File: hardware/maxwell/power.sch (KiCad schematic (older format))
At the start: 50 parts, among them J7 Dynamo Input, J9 Battery, Q2 PSMN5R4-25YLD, Q3 DMG9926UDM, Q4 NTR1P02T1, Q5 NTR1P02T1, U1 MCP1501, U10 MIC39102, U11 AP9101C-SOT-25, U12 INA219AID, U13 PCF8593, U3 TPS2113, U4 PCA9536D, U6 AD7991, U8 TLP188, U9 Buck Regulator

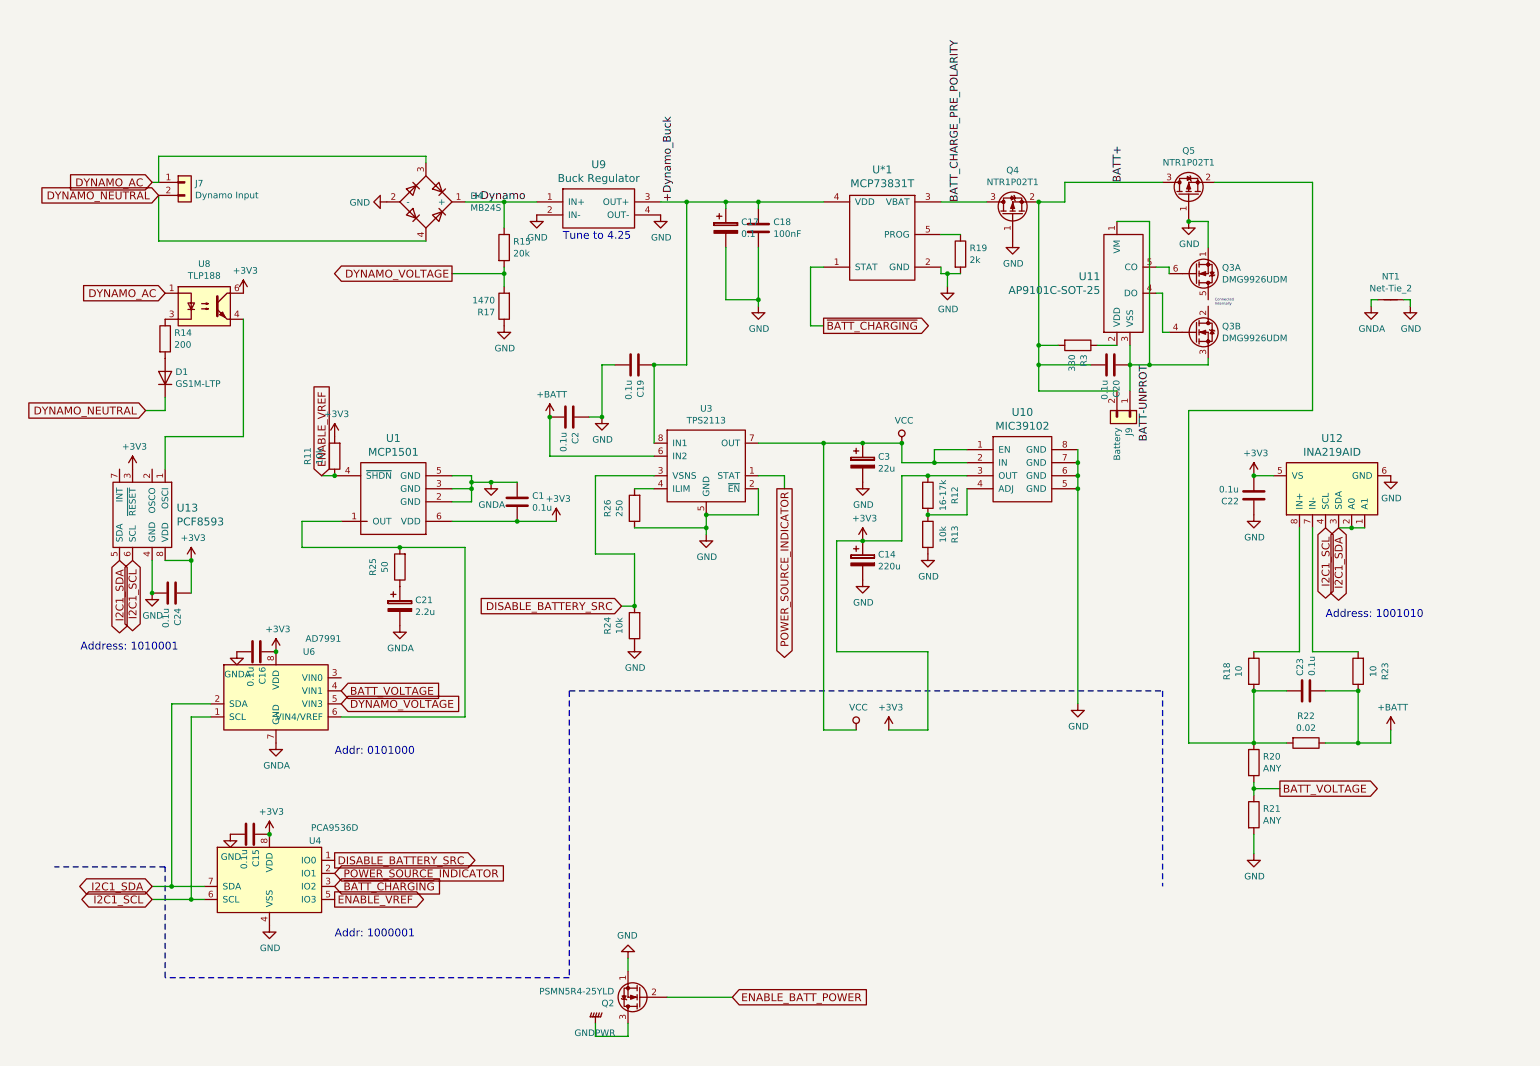
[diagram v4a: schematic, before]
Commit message: Revision 1.8a
* Collects regulated dynamo voltage via ADC channel 0.
* Swaps default power source from VBATT to VDYNAMO.  When charging, the
battery may have exactly the same voltage as the dynamo due to voltage
pulldown.  During such a scenario, we should use the dynamo.
* Adds previously missing pulldown resistor for open drain speed
input.
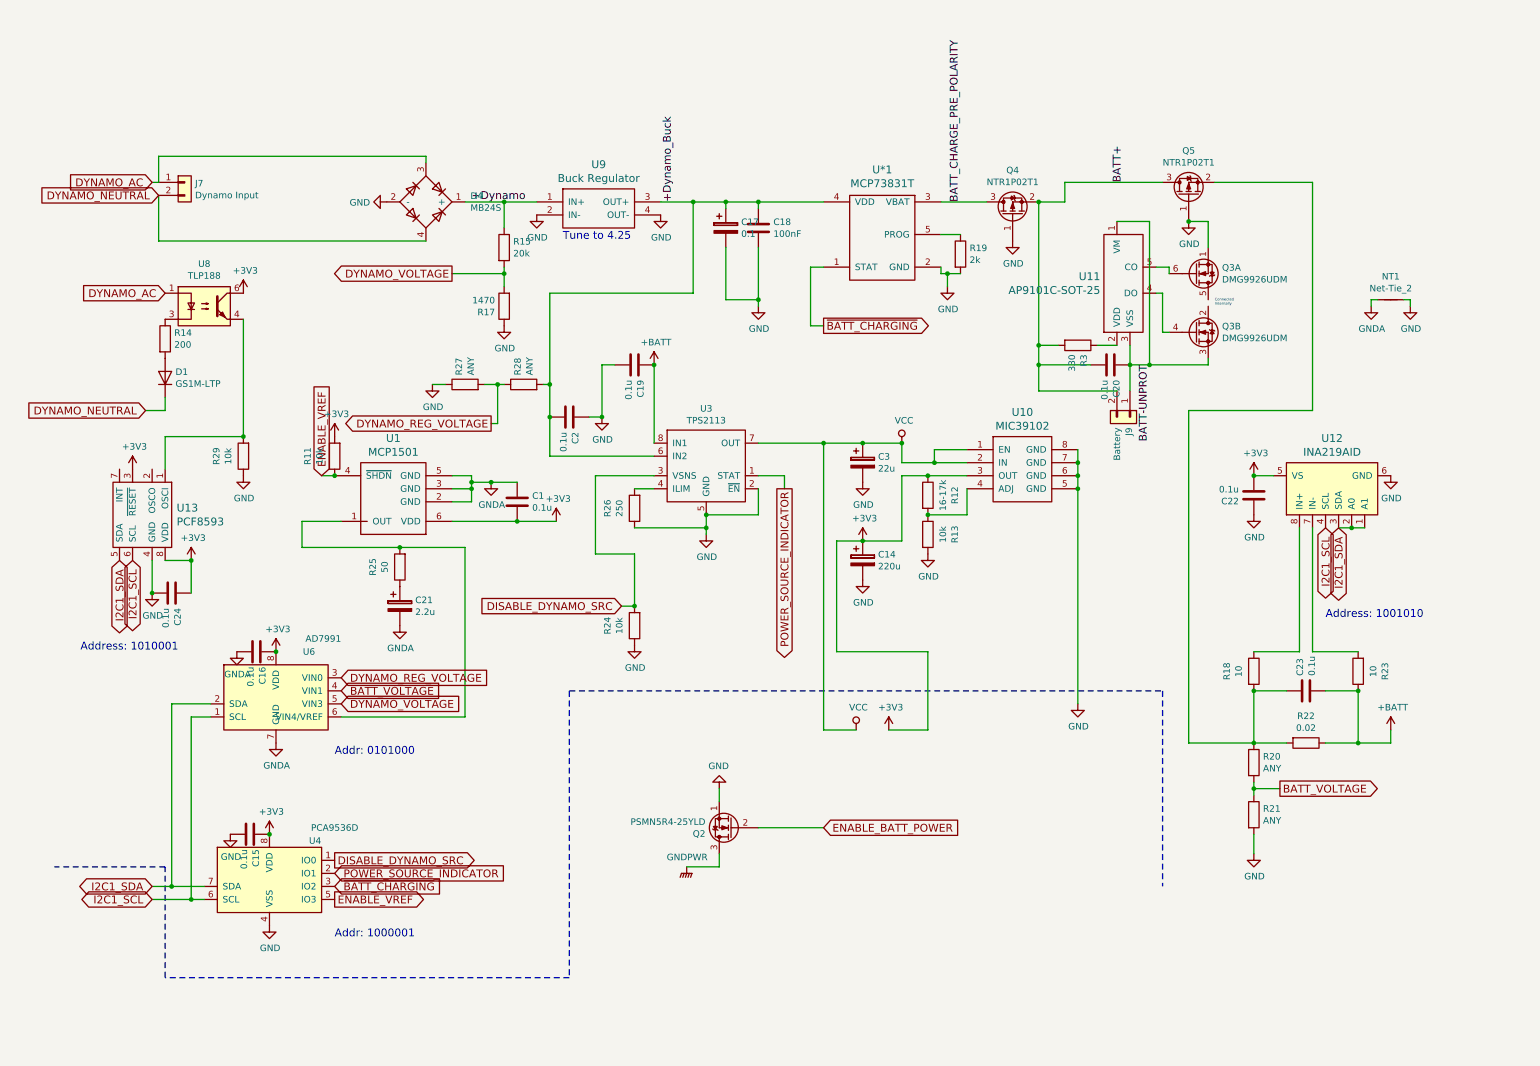
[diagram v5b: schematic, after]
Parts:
- added R27, R28: ANY, coddingtonbear:0805_Milling, symbol maxwell-rescue:R-RESCUE-maxwell
- added R29: 10k, coddingtonbear:0805_Milling, symbol maxwell-rescue:R-RESCUE-maxwell
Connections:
- net +BATT: now also C19.2, U3.8 (IN1); no longer C2.1, U3.6 (IN2)
- net +Dynamo_Buck: now also C2.1, U3.6 (IN2), R28.2; no longer C19.2, U3.8 (IN1)
- net GND: now also R27.1, R29.1
- net at U13.1 (OSCI), U8.4: now also R29.2
- net DYNAMO_REG_VOLTAGE: now reaches U6.3 (VIN0)
- net DYNAMO_REG_VOLTAGE: now also R27.2, R28.1
- net DISABLE_BATTERY_SRC renamed DISABLE_DYNAMO_SRC
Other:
- moved on the sheet: Q2
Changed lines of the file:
@@
 $EndComp
 Wire Wire Line
-	4900 7650 4650 7650
-Wire Wire Line
-	4650 7650 4650 7550
-Wire Wire Line
-	4900 7550 4900 7650
-Text GLabel 5700 7350 2    60   Input ~ 0
+	5600 6350 5350 6350
+Wire Wire Line
+	5600 6250 5600 6350
+Text GLabel 6400 6050 2    60   Input ~ 0
 ENABLE_BATT_POWER
 $Comp
 L maxwell-rescue:GND-RESCUE-maxwell #PWR050
 U 1 1 5A2580F1
-P 4900 7050
-F 0 "#PWR050" H 4900 6800 50  0001 C CNN
-F 1 "GND" H 4905 6877 50  0000 C CNN
-F 2 "" H 4900 7050 50  0001 C CNN
-F 3 "" H 4900 7050 50  0001 C CNN
-	1    4900 7050
+P 5600 5750
+F 0 "#PWR050" H 5600 5500 50  0001 C CNN
+F 1 "GND" H 5605 5577 50  0000 C CNN
+F 2 "" H 5600 5750 50  0001 C CNN
+F 3 "" H 5600 5750 50  0001 C CNN
+	1    5600 5750
 	-1   0    0    1
 $EndComp
@@
 L maxwell-rescue:GNDPWR-RESCUE-maxwell #PWR049
 U 1 1 5A25809F
-P 4650 7550
-F 0 "#PWR049" H 4650 7350 50  0001 C CNN
-F 1 "GNDPWR" H 4654 7624 50  0000 C CNN
-F 2 "" H 4650 7500 50  0001 C CNN
-F 3 "" H 4650 7500 50  0001 C CNN
-	1    4650 7550
-	-1   0    0    1
+P 5350 6350
+F 0 "#PWR049" H 5350 6150 50  0001 C CNN
+F 1 "GNDPWR" H 5354 6424 50  0000 C CNN
+F 2 "" H 5350 6300 50  0001 C CNN
+F 3 "" H 5350 6300 50  0001 C CNN
+	1    5350 6350
+	1    0    0    -1
 $EndComp
 $Comp
 L maxwell-rescue:Q_NMOS_SGD-device Q2
 U 1 1 5A87E051
-P 5000 7350
-F 0 "Q2" H 5206 7396 50  0000 L CNN
-F 1 "PSMN5R4-25YLD" H 5206 7305 50  0000 L CNN
-F 2 "coddingtonbear:PSMN5R4-25YLD" H 5200 7450 50  0001 C CNN
-F 3 "" H 5000 7350 50  0001 C CNN
-	1    5000 7350
+P 5700 6050
+F 0 "Q2" H 5906 6096 50  0000 L CNN
+F 1 "PSMN5R4-25YLD" H 5906 6005 50  0000 L CNN
+F 2 "coddingtonbear:PSMN5R4-25YLD" H 5900 6150 50  0001 C CNN
+F 3 "" H 5700 6050 50  0001 C CNN
+	1    5700 6050
 	-1   0    0    1
 $EndComp
@@
 L maxwell-rescue:+BATT-RESCUE-maxwell #PWR037
 U 1 1 5A884C49
-P 4300 2900
-F 0 "#PWR037" H 4300 2750 50  0001 C CNN
-F 1 "+BATT" H 4315 3073 50  0000 C CNN
-F 2 "" H 4300 2900 50  0001 C CNN
-F 3 "" H 4300 2900 50  0001 C CNN
-	1    4300 2900
+P 5100 2500
+F 0 "#PWR037" H 5100 2350 50  0001 C CNN
+F 1 "+BATT" H 5115 2673 50  0000 C CNN
+F 2 "" H 5100 2500 50  0001 C CNN
+F 3 "" H 5100 2500 50  0001 C CNN
+	1    5100 2500
 	1    0    0    -1
 $EndComp
@@
 $EndComp
 Wire Wire Line
-	4900 7150 4900 7050
-Wire Wire Line
-	5700 7350 5200 7350
+	5600 5850 5600 5750
+Wire Wire Line
+	6400 6050 5900 6050
 Wire Wire Line
 	1300 900  3350 900
@@
 Connection ~ 4700 2900
 Text GLabel 2650 6300 2    60   Output ~ 0
-DISABLE_BATTERY_SRC
+DISABLE_DYNAMO_SRC
 Text GLabel 4850 4350 0    60   Input ~ 0
-DISABLE_BATTERY_SRC
-Wire Wire Line
-	5150 1250 5350 1250
-Connection ~ 5100 2500
-Connection ~ 5350 1250
-Wire Wire Line
-	5350 1250 5650 1250
-Wire Wire Line
-	5350 2500 5100 2500
-Wire Wire Line
-	5350 1250 5350 2500
+DISABLE_DYNAMO_SRC
 Connection ~ 4300 2900
 $Comp
@@
 	9200 5400 9700 5400
 $Comp
-L maxwell-rescue:+3V3-RESCUE-maxwell #PWR?
+L maxwell-rescue:+3V3-RESCUE-maxwell #PWR0143
 U 1 1 5C37AAA7
 P 1100 3300
-F 0 "#PWR?" H 1100 3150 50  0001 C CNN
+F 0 "#PWR0143" H 1100 3150 50  0001 C CNN
 F 1 "+3V3" H 1115 3473 50  0000 C CNN
 F 2 "" H 1100 3300 50  0001 C CNN
@@
 	1    0    0    -1
 $EndComp
+Wire Wire Line
+	5150 1250 5400 1250
+Wire Wire Line
+	4300 2900 4300 2650
+Wire Wire Line
+	4300 1950 5400 1950
+Wire Wire Line
+	5400 1950 5400 1250
+Connection ~ 5400 1250
+Wire Wire Line
+	5400 1250 5650 1250
+Connection ~ 5100 2500
+$Comp
+L maxwell-rescue:R-RESCUE-maxwell R28
+U 1 1 5C56CC7D
+P 4100 2650
+F 0 "R28" H 4170 2696 50  0000 L CNN
+F 1 "ANY" H 4170 2605 50  0000 L CNN
+F 2 "coddingtonbear:0805_Milling" V 4030 2650 50  0001 C CNN
+F 3 "" H 4100 2650 50  0001 C CNN
+	1    4100 2650
+	0    -1   -1   0
+$EndComp
+$Comp
+L maxwell-rescue:R-RESCUE-maxwell R27
+U 1 1 5C56CDED
+P 3650 2650
+F 0 "R27" H 3720 2696 50  0000 L CNN
+F 1 "ANY" H 3720 2605 50  0000 L CNN
+F 2 "coddingtonbear:0805_Milling" V 3580 2650 50  0001 C CNN
+F 3 "" H 3650 2650 50  0001 C CNN
+	1    3650 2650
+	0    -1   -1   0
+$EndComp
+$Comp
+L maxwell-rescue:GND-RESCUE-maxwell #PWR0144
+U 1 1 5C56CE75
+P 3400 2650
+F 0 "#PWR0144" H 3400 2400 50  0001 C CNN
+F 1 "GND" H 3405 2477 50  0000 C CNN
+F 2 "" H 3400 2650 50  0001 C CNN
+F 3 "" H 3400 2650 50  0001 C CNN
+	1    3400 2650
+	1    0    0    -1
+$EndComp
+Text GLabel 3850 2950 0    60   Output ~ 0
+DYNAMO_REG_VOLTAGE
+Wire Wire Line
+	3400 2650 3500 2650
+Wire Wire Line
+	3800 2650 3900 2650
+Wire Wire Line
+	4250 2650 4300 2650
+Connection ~ 4300 2650
+Wire Wire Line
+	4300 2650 4300 1950
+Wire Wire Line
+	3850 2950 3900 2950
+Wire Wire Line
+	3900 2950 3900 2650
+Connection ~ 3900 2650
+Wire Wire Line
+	3900 2650 3950 2650
+Text GLabel 2700 4900 2    60   Input ~ 0
+DYNAMO_REG_VOLTAGE
+$Comp
+L maxwell-rescue:R-RESCUE-maxwell R29
+U 1 1 5C58DE09
+P 1950 3200
+F 0 "R29" V 2157 3200 50  0000 C CNN
+F 1 "10k" V 2066 3200 50  0000 C CNN
+F 2 "coddingtonbear:0805_Milling" V 1880 3200 50  0001 C CNN
+F 3 "" H 1950 3200 50  0001 C CNN
+	1    1950 3200
+	-1   0    0    1
+$EndComp
+Connection ~ 1950 3050
+$Comp
+L maxwell-rescue:GND-RESCUE-maxwell #PWR0145
+U 1 1 5C58DEA9
+P 1950 3350
+F 0 "#PWR0145" H 1950 3100 50  0001 C CNN
+F 1 "GND" H 1955 3177 50  0000 C CNN
+F 2 "" H 1950 3350 50  0001 C CNN
+F 3 "" H 1950 3350 50  0001 C CNN
+	1    1950 3350
+	1    0    0    -1
+$EndComp

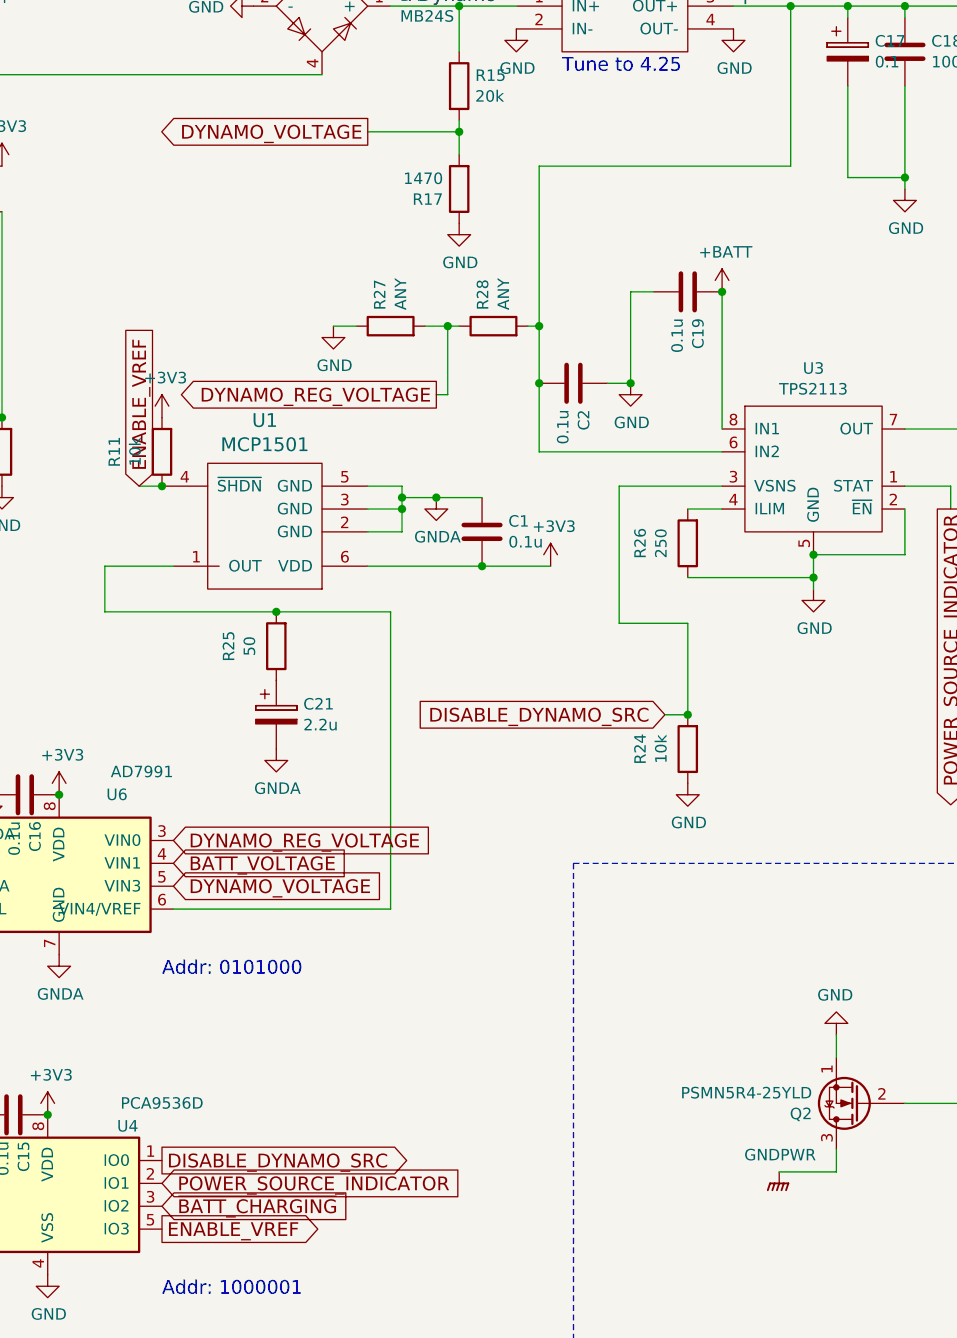
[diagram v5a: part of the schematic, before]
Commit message: Updating to 1.8b; re-assigns power sources-to-TPS chip reverting earlier changes.
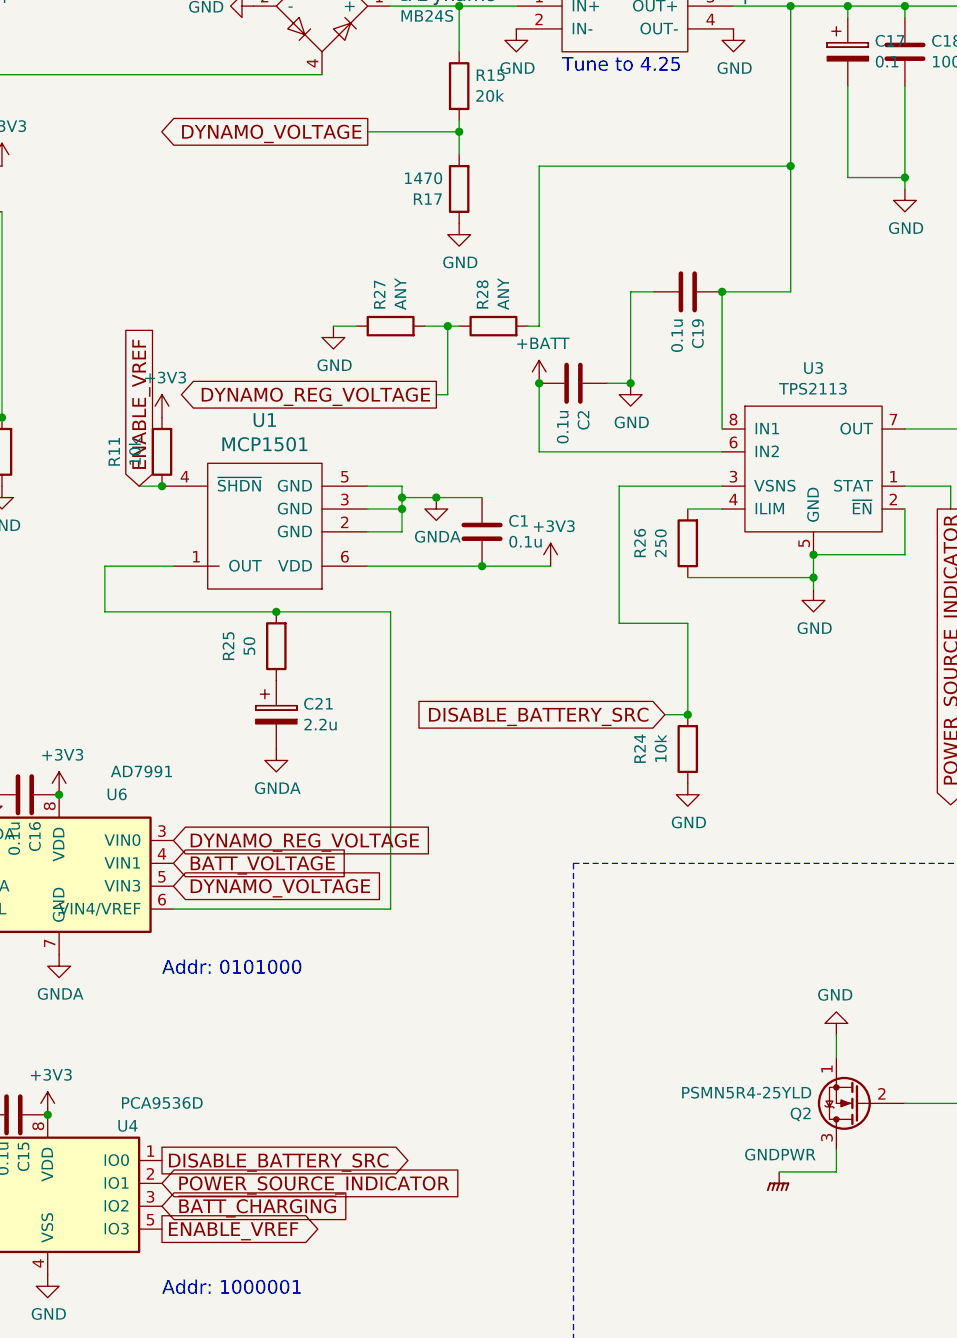
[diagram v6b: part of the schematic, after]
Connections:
- net +BATT: now also C2.1, U3.6 (IN2); no longer C19.2, U3.8 (IN1)
- net +Dynamo_Buck: now also C19.2, U3.8 (IN1); no longer C2.1, U3.6 (IN2)
- net DISABLE_DYNAMO_SRC renamed DISABLE_BATTERY_SRC
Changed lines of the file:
@@
 L maxwell-rescue:+BATT-RESCUE-maxwell #PWR037
 U 1 1 5A884C49
-P 5100 2500
-F 0 "#PWR037" H 5100 2350 50  0001 C CNN
-F 1 "+BATT" H 5115 2673 50  0000 C CNN
-F 2 "" H 5100 2500 50  0001 C CNN
-F 3 "" H 5100 2500 50  0001 C CNN
-	1    5100 2500
+P 4300 2900
+F 0 "#PWR037" H 4300 2750 50  0001 C CNN
+F 1 "+BATT" H 4315 3073 50  0000 C CNN
+F 2 "" H 4300 2900 50  0001 C CNN
+F 3 "" H 4300 2900 50  0001 C CNN
+	1    4300 2900
 	1    0    0    -1
 $EndComp
@@
 Connection ~ 4700 2900
 Text GLabel 2650 6300 2    60   Output ~ 0
-DISABLE_DYNAMO_SRC
+DISABLE_BATTERY_SRC
 Text GLabel 4850 4350 0    60   Input ~ 0
-DISABLE_DYNAMO_SRC
-Connection ~ 4300 2900
+DISABLE_BATTERY_SRC
 $Comp
 L power:GNDA #PWR0112
@@
 	5150 1250 5400 1250
 Wire Wire Line
-	4300 2900 4300 2650
-Wire Wire Line
 	4300 1950 5400 1950
 Wire Wire Line
@@
 Wire Wire Line
 	4250 2650 4300 2650
-Connection ~ 4300 2650
 Wire Wire Line
 	4300 2650 4300 1950
@@
 	1    0    0    -1
 $EndComp
+Connection ~ 4300 2900
+Wire Wire Line
+	5100 2500 5400 2500
+Wire Wire Line
+	5400 2500 5400 1950
+Connection ~ 5400 1950
 $EndSCHEMATC
